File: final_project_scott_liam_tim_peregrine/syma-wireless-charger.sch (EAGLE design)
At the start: 46 parts, among them U1 SAMD21E

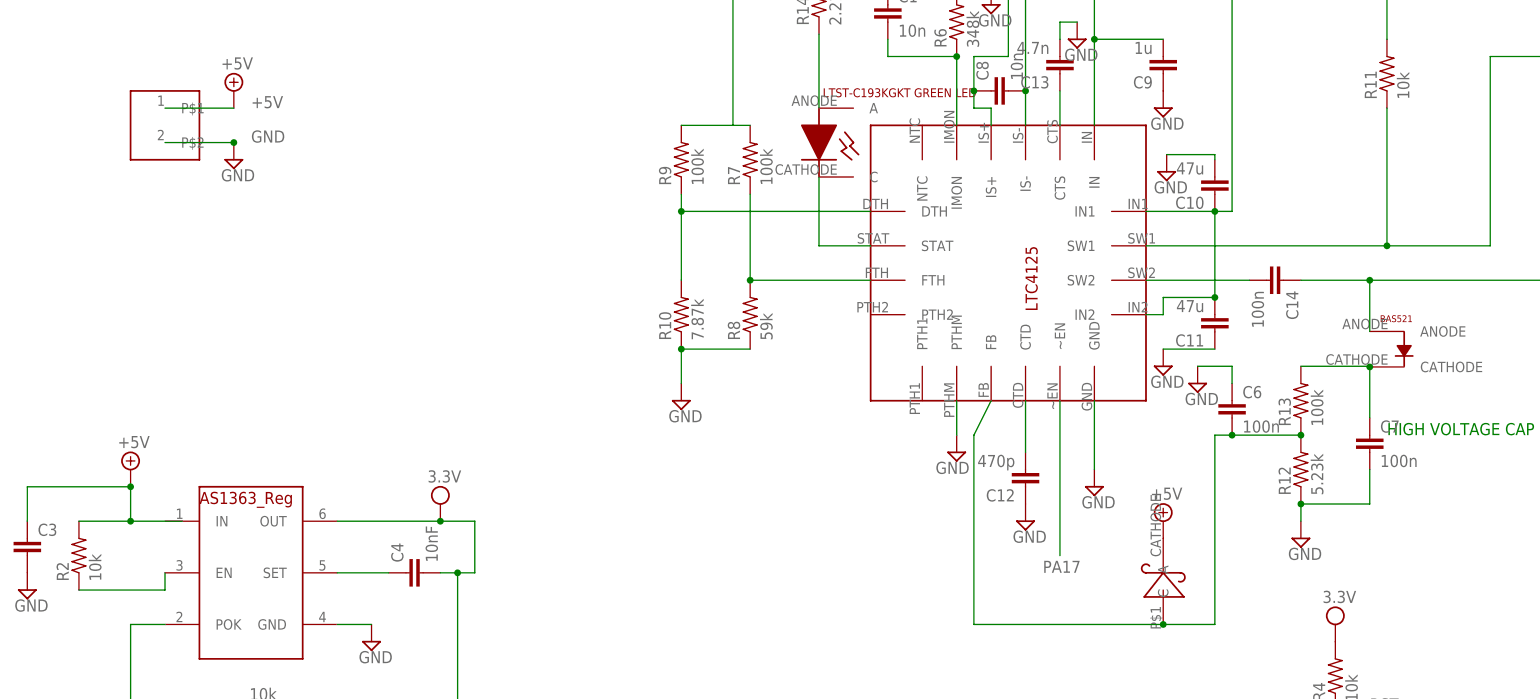
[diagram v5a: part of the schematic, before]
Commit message: Fixed some packages
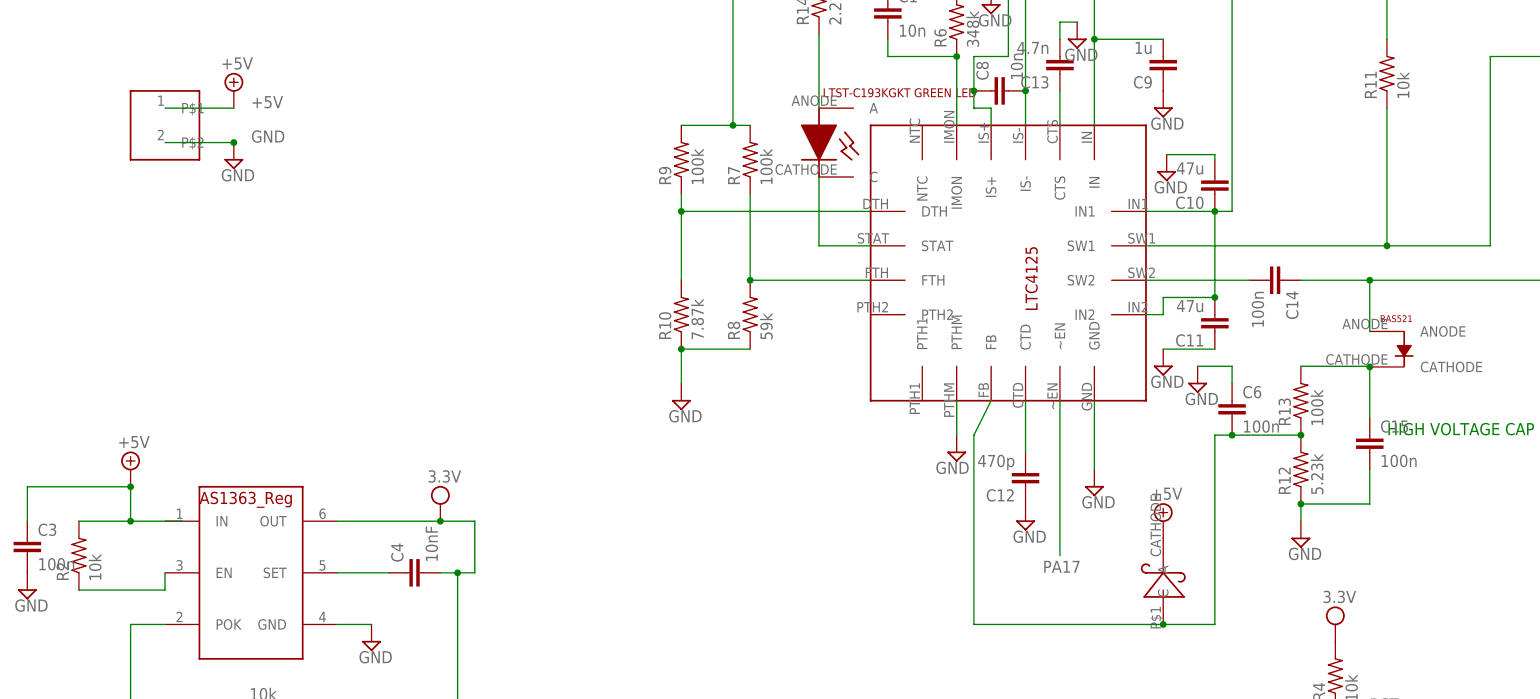
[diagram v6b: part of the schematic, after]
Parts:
- removed C7: 100n, rcl:C-EUC0805
- added C15: 100n, resistor:C-EUC0603
- C14: device rcl:C-EUC0805 -> rcl:C-EUC1206
- C3: value (none) -> 100n
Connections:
- net GND: now also C15.2; no longer C7.2
- net N$10: now also C15.1; no longer C7.1
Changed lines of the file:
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@@
 <grid distance="0.1" unitdist="inch" unit="inch" style="lines" multiple="1" display="no" altdistance="0.01" altunitdist="inch" altunit="inch"/>
 <layers>
-<layer number="1" name="Top" color="4" fill="1" visible="no" active="no"/>
-<layer number="16" name="Bottom" color="1" fill="1" visible="no" active="no"/>
-<layer number="17" name="Pads" color="2" fill="1" visible="no" active="no"/>
-<layer number="18" name="Vias" color="2" fill="1" visible="no" active="no"/>
-<layer number="19" name="Unrouted" color="6" fill="1" visible="no" active="no"/>
-<layer number="20" name="Dimension" color="15" fill="1" visible="no" active="no"/>
-<layer number="21" name="tPlace" color="7" fill="1" visible="no" active="no"/>
-<layer number="22" name="bPlace" color="7" fill="1" visible="no" active="no"/>
-<layer number="23" name="tOrigins" color="15" fill="1" visible="no" active="no"/>
-<layer number="24" name="bOrigins" color="15" fill="1" visible="no" active="no"/>
-<layer number="25" name="tNames" color="7" fill="1" visible="no" active="no"/>
-<layer number="26" name="bNames" color="7" fill="1" visible="no" active="no"/>
-<layer number="27" name="tValues" color="7" fill="1" visible="no" active="no"/>
-<layer number="28" name="bValues" color="7" fill="1" visible="no" active="no"/>
+<layer number="1" name="Top" color="4" fill="1" visible="yes" active="no"/>
+<layer number="16" name="Bottom" color="1" fill="1" visible="yes" active="no"/>
+<layer number="17" name="Pads" color="2" fill="1" visible="yes" active="no"/>
+<layer number="18" name="Vias" color="2" fill="1" visible="yes" active="no"/>
+<layer number="19" name="Unrouted" color="6" fill="1" visible="yes" active="no"/>
+<layer number="20" name="Dimension" color="15" fill="1" visible="yes" active="no"/>
+<layer number="21" name="tPlace" color="7" fill="1" visible="yes" active="no"/>
+<layer number="22" name="bPlace" color="7" fill="1" visible="yes" active="no"/>
+<layer number="23" name="tOrigins" color="15" fill="1" visible="yes" active="no"/>
+<layer number="24" name="bOrigins" color="15" fill="1" visible="yes" active="no"/>
+<layer number="25" name="tNames" color="7" fill="1" visible="yes" active="no"/>
+<layer number="26" name="bNames" color="7" fill="1" visible="yes" active="no"/>
+<layer number="27" name="tValues" color="7" fill="1" visible="yes" active="no"/>
+<layer number="28" name="bValues" color="7" fill="1" visible="yes" active="no"/>
 <layer number="29" name="tStop" color="7" fill="3" visible="no" active="no"/>
 <layer number="30" name="bStop" color="7" fill="6" visible="no" active="no"/>
@@
 <layer number="35" name="tGlue" color="7" fill="4" visible="no" active="no"/>
 <layer number="36" name="bGlue" color="7" fill="5" visible="no" active="no"/>
-<layer number="37" name="tTest" color="7" fill="1" visible="no" active="no"/>
-<layer number="38" name="bTest" color="7" fill="1" visible="no" active="no"/>
+<layer number="37" name="tTest" color="7" fill="1" visible="yes" active="no"/>
+<layer number="38" name="bTest" color="7" fill="1" visible="yes" active="no"/>
 <layer number="39" name="tKeepout" color="4" fill="11" visible="no" active="no"/>
 <layer number="40" name="bKeepout" color="1" fill="11" visible="no" active="no"/>
@@
 <layer number="44" name="Drills" color="7" fill="1" visible="no" active="no"/>
 <layer number="45" name="Holes" color="7" fill="1" visible="no" active="no"/>
-<layer number="46" name="Milling" color="3" fill="1" visible="no" active="no"/>
-<layer number="47" name="Measures" color="7" fill="1" visible="no" active="no"/>
-<layer number="48" name="Document" color="7" fill="1" visible="no" active="no"/>
-<layer number="49" name="Reference" color="7" fill="1" visible="no" active="no"/>
-<layer number="51" name="tDocu" color="7" fill="1" visible="no" active="no"/>
-<layer number="52" name="bDocu" color="7" fill="1" visible="no" active="no"/>
+<layer number="46" name="Milling" color="3" fill="1" visible="yes" active="no"/>
+<layer number="47" name="Measures" color="7" fill="1" visible="yes" active="no"/>
+<layer number="48" name="Document" color="7" fill="1" visible="yes" active="no"/>
+<layer number="49" name="Reference" color="7" fill="1" visible="yes" active="no"/>
+<layer number="51" name="tDocu" color="7" fill="1" visible="yes" active="no"/>
+<layer number="52" name="bDocu" color="7" fill="1" visible="yes" active="no"/>
 <layer number="90" name="Modules" color="5" fill="1" visible="yes" active="yes"/>
 <layer number="91" name="Nets" color="2" fill="1" visible="yes" active="yes"/>
@@
 <part name="C2" library="resistor" deviceset="C-EU" device="C0805K" value="100nF"/>
 <part name="U2" library="foe-scale" deviceset="3.3V_AS1363" device=""/>
-<part name="C3" library="resistor" deviceset="C-EU" device="C0805K"/>
+<part name="C3" library="resistor" deviceset="C-EU" device="C0805K" value="100n"/>
 <part name="U$3" library="foe-scale" deviceset="1X02" device=""/>
 <part name="SUPPLY1" library="supply2" deviceset="+5V" device=""/>
@@
 <part name="SUPPLY18" library="supply2" deviceset="GND" device=""/>
 <part name="C6" library="rcl" deviceset="C-EU" device="C0805" value="100n"/>
-<part name="C7" library="rcl" deviceset="C-EU" device="C0805" value="100n"/>
 <part name="U$2" library="foe-scale" deviceset="BAS521" device=""/>
 <part name="U$4" library="foe-scale" deviceset="RGBLED" device=""/>
@@
 <part name="SUPPLY30" library="supply2" deviceset="VDD" device="" value="3.3V"/>
 <part name="SUPPLY31" library="supply2" deviceset="VDD" device="" value="3.3V"/>
-<part name="C14" library="rcl" deviceset="C-EU" device="C0805" value="100n"/>
+<part name="C14" library="rcl" deviceset="C-EU" device="C1206" value="100n"/>
 <part name="U$8" library="foe-scale" deviceset="SCHTKYDIODE-523" device=""/>
 <part name="SUPPLY32" library="supply2" deviceset="+5V" device=""/>
@@
 <part name="U$11" library="foe-scale" deviceset="1X02" device=""/>
 <part name="U$9" library="foe-scale" deviceset="LTST-C193KGKT_GREEN-LED" device=""/>
+<part name="C15" library="resistor" deviceset="C-EU" device="C0603" value="100n"/>
 </parts>
 <sheets>
@@
 <instance part="SUPPLY18" gate="GND" x="35.56" y="99.06"/>
 <instance part="C6" gate="G$1" x="71.12" y="40.64"/>
-<instance part="C7" gate="G$1" x="91.44" y="35.56"/>
 <instance part="U$2" gate="G$1" x="91.44" y="47.244"/>
 <instance part="U$4" gate="G$1" x="101.6" y="-53.34" rot="R90"/>
@@
 <instance part="U$11" gate="G$1" x="137.16" y="88.9"/>
 <instance part="U$9" gate="G$1" x="7.62" y="78.74"/>
+<instance part="C15" gate="G$1" x="91.44" y="35.56"/>
 </instances>
 <busses>
@@
 </segment>
 <segment>
-<pinref part="C7" gate="G$1" pin="2"/>
 <wire x1="91.44" y1="30.48" x2="91.44" y2="25.4" width="0.1524" layer="91"/>
 <pinref part="R12" gate="G$1" pin="1"/>
@@
 <wire x1="81.28" y1="22.86" x2="81.28" y2="25.4" width="0.1524" layer="91"/>
 <junction x="81.28" y="25.4"/>
+<pinref part="C15" gate="G$1" pin="2"/>
 </segment>
 </net>
@@
 <pinref part="R13" gate="G$1" pin="2"/>
 <wire x1="81.28" y1="45.72" x2="91.44" y2="45.72" width="0.1524" layer="91"/>
-<pinref part="C7" gate="G$1" pin="1"/>
 <wire x1="91.44" y1="45.72" x2="91.44" y2="45.624" width="0.1524" layer="91"/>
 <pinref part="U$2" gate="G$1" pin="CATHODE"/>
 <wire x1="91.44" y1="45.624" x2="91.44" y2="38.1" width="0.1524" layer="91"/>
 <junction x="91.44" y="45.624"/>
+<pinref part="C15" gate="G$1" pin="1"/>
 </segment>
 </net>
@@
 <junction x="10.16" y="116.84"/>
 <pinref part="R14" gate="G$1" pin="2"/>
-</segment>
-</net>
+<junction x="-2.54" y="81.28"/>
+</segment>
+</net>
